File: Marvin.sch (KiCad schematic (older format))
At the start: 19 parts, among them J1 Arduino_Mega_Header, M1 Motor_DC, M2 Stepper_Motor_bipolar, M3 Stepper_Motor_bipolar, M4 Motor_DC, SW1 Rotary_Encoder, U1 L7805, U2 RoetzerRegler, U3 DM420, U4 DM420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

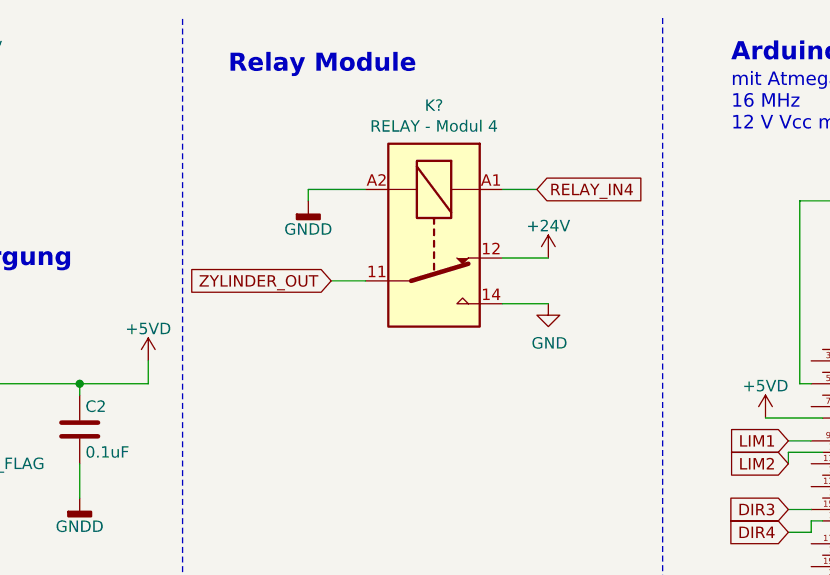
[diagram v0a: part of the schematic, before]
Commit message: Kommentar
Kommentar bei Releis Modul nachgetragen
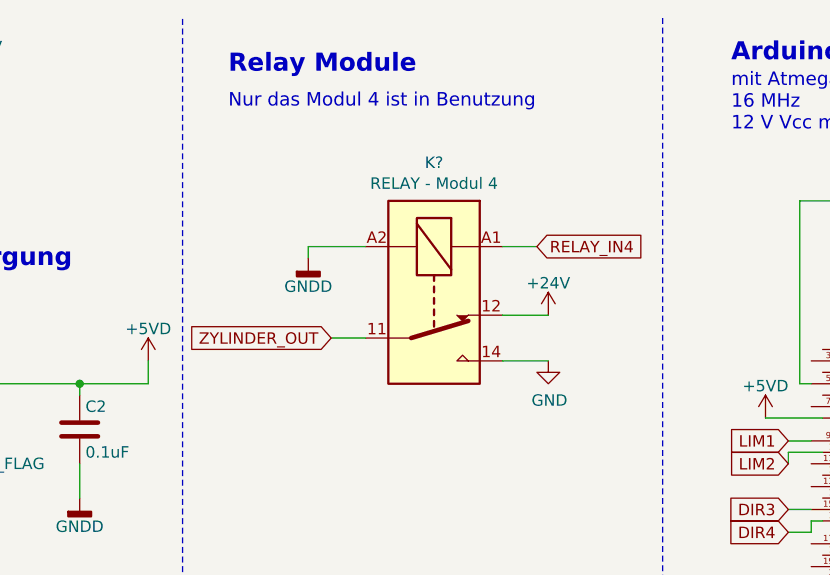
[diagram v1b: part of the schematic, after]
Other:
- note added: "Nur das Modul 4 ist in Benutzung"
- moved on the sheet: K?
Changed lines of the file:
@@
 L Relay:FINDER-32.21-x000 K?
 U 1 1 5C813E0F
-P 3950 1450
-F 0 "K?" V 3383 1450 50  0000 C CNN
-F 1 "RELAY - Modul 4" V 3474 1450 50  0000 C CNN
-F 2 "Relay_THT:Relay_SPST_Finder_32.21-x300" H 5220 1420 50  0001 C CNN
-F 3 "https://gfinder.findernet.com/assets/Series/355/S32EN.pdf" H 3950 1450 50  0001 C CNN
-	1    3950 1450
+P 3950 1700
+F 0 "K?" V 3383 1700 50  0000 C CNN
+F 1 "RELAY - Modul 4" V 3474 1700 50  0000 C CNN
+F 2 "Relay_THT:Relay_SPST_Finder_32.21-x300" H 5220 1670 50  0001 C CNN
+F 3 "https://gfinder.findernet.com/assets/Series/355/S32EN.pdf" H 3950 1700 50  0001 C CNN
+	1    3950 1700
 	0    1    1    0
 $EndComp
@@
 Wire Wire Line
 	6650 4050 6750 4050
-Text GLabel 4400 1250 2    50   Input ~ 0
+Text GLabel 4400 1500 2    50   Input ~ 0
 RELAY_IN4
 Wire Wire Line
-	4250 1250 4400 1250
+	4250 1500 4400 1500
 Wire Wire Line
-	3650 1250 3400 1250
+	3650 1500 3400 1500
 Wire Wire Line
-	3400 1250 3400 1300
+	3400 1500 3400 1550
 $Comp
 L Marvin-rescue:GNDD-power #PWR?
 U 1 1 5C824BEE
-P 3400 1300
-F 0 "#PWR?" H 3400 1050 50  0001 C CNN
-F 1 "GNDD" H 3400 1175 50  0000 C CNN
-F 2 "" H 3400 1300 50  0001 C CNN
-F 3 "" H 3400 1300 50  0001 C CNN
-	1    3400 1300
+P 3400 1550
+F 0 "#PWR?" H 3400 1300 50  0001 C CNN
+F 1 "GNDD" H 3400 1425 50  0000 C CNN
+F 2 "" H 3400 1550 50  0001 C CNN
+F 3 "" H 3400 1550 50  0001 C CNN
+	1    3400 1550
 	1    0    0    -1
 $EndComp
@@
 L Marvin-rescue:+24V-power #PWR?
 U 1 1 5C824C1F
-P 4450 1550
-F 0 "#PWR?" H 4450 1400 50  0001 C CNN
-F 1 "+24V" H 4450 1690 50  0000 C CNN
-F 2 "" H 4450 1550 50  0001 C CNN
-F 3 "" H 4450 1550 50  0001 C CNN
-	1    4450 1550
+P 4450 1800
+F 0 "#PWR?" H 4450 1650 50  0001 C CNN
+F 1 "+24V" H 4450 1940 50  0000 C CNN
+F 2 "" H 4450 1800 50  0001 C CNN
+F 3 "" H 4450 1800 50  0001 C CNN
+	1    4450 1800
 	1    0    0    -1
 $EndComp
 Wire Wire Line
-	4450 1550 4250 1550
+	4450 1800 4250 1800
 $Comp
 L power:GND #PWR?
 U 1 1 5C82A8E7
-P 4450 1750
-F 0 "#PWR?" H 4450 1500 50  0001 C CNN
-F 1 "GND" H 4455 1577 50  0000 C CNN
-F 2 "" H 4450 1750 50  0001 C CNN
-F 3 "" H 4450 1750 50  0001 C CNN
-	1    4450 1750
+P 4450 2000
+F 0 "#PWR?" H 4450 1750 50  0001 C CNN
+F 1 "GND" H 4455 1827 50  0000 C CNN
+F 2 "" H 4450 2000 50  0001 C CNN
+F 3 "" H 4450 2000 50  0001 C CNN
+	1    4450 2000
 	1    0    0    -1
 $EndComp
 Wire Wire Line
-	4250 1750 4450 1750
-Text GLabel 3500 1650 0    50   Input ~ 0
+	4250 2000 4450 2000
+Text GLabel 3500 1900 0    50   Input ~ 0
 ZYLINDER_OUT
 Wire Wire Line
-	3650 1650 3500 1650
+	3650 1900 3500 1900
 Wire Notes Line
 	2850 3050 2850 500
 Text Notes 3050 750  0    79   ~ 16
 Relay Module
+Text Notes 3050 900  0    59   ~ 0
+Nur das Modul 4 ist in Benutzung
 $EndSCHEMATC

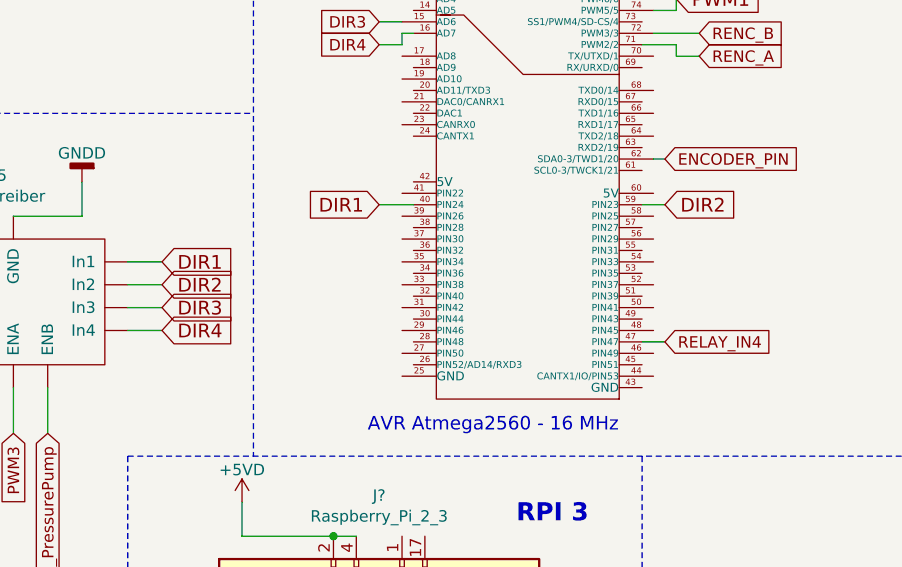
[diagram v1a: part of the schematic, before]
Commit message: IN1 & IN2 ausgetauscht mit DIR1 & DIR2
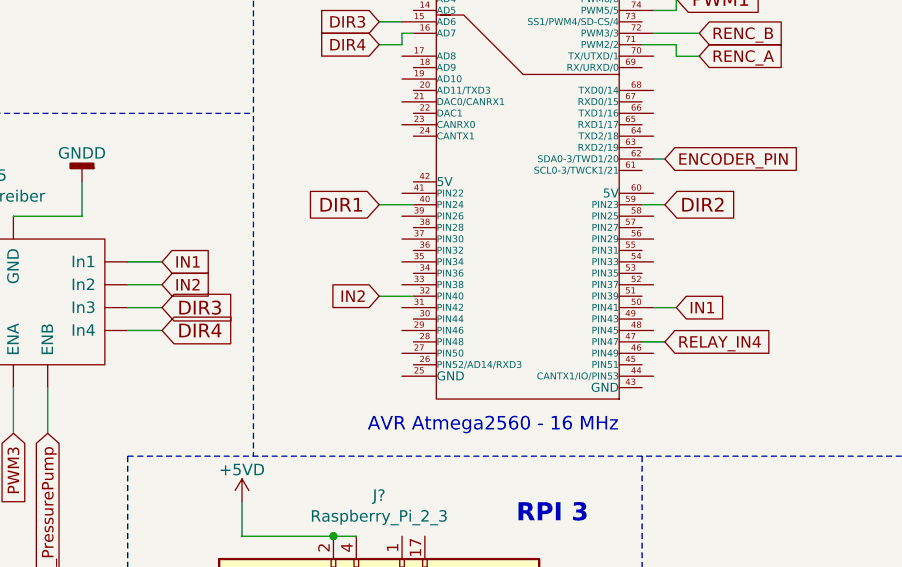
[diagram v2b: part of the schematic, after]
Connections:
- net DIR1: no longer U5.~ (Vcc)
- net DIR2: no longer U5.~ (Vcc)
- net IN2: now reaches J1.32 (PIN40)
- net IN2: now also U5.~ (Vcc)
- net IN1: now reaches J1.50 (PIN41)
- net IN1: now also U5.~ (Vcc)
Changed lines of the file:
@@
 Wire Wire Line
 	3800 4300 3800 4250
-Text GLabel 4550 3800 2    60   Input ~ 0
-DIR2
-Text GLabel 4550 3700 2    60   Input ~ 0
-DIR1
 Text GLabel 4550 3900 2    60   Input ~ 0
 DIR3
@@
 Text Notes 3050 900  0    59   ~ 0
 Nur das Modul 4 ist in Benutzung
+Text GLabel 6800 3900 2    50   Input ~ 0
+IN1
+Text GLabel 5500 3850 0    50   Input ~ 0
+IN2
+Wire Wire Line
+	5500 3850 5650 3850
+Wire Wire Line
+	6800 3900 6700 3900
+Text GLabel 4550 3700 2    50   Input ~ 0
+IN1
+Text GLabel 4550 3800 2    50   Input ~ 0
+IN2
 $EndSCHEMATC
